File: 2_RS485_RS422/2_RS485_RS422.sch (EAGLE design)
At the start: 16 parts, among them IC1 74HCT02D, IC2 MAX485CSA, IC3 MAX485CSA, IC4 MAX489CSD, X1 AKL18X-10W, X8 ALLSERIALD

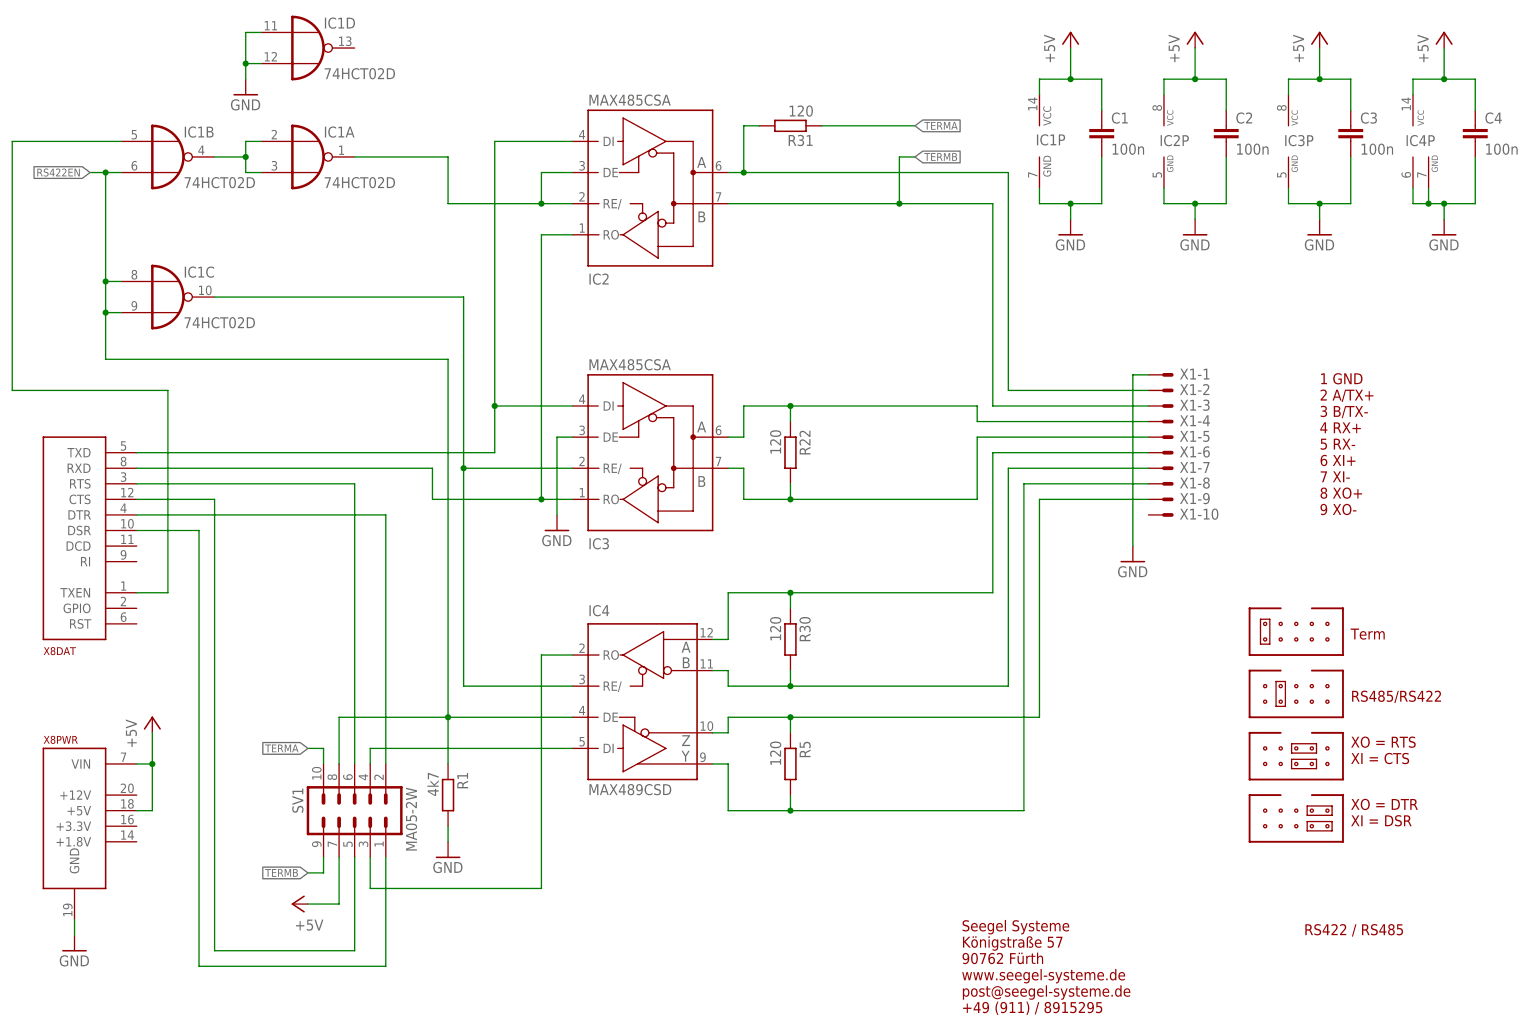
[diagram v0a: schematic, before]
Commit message: finish RS485 PCB
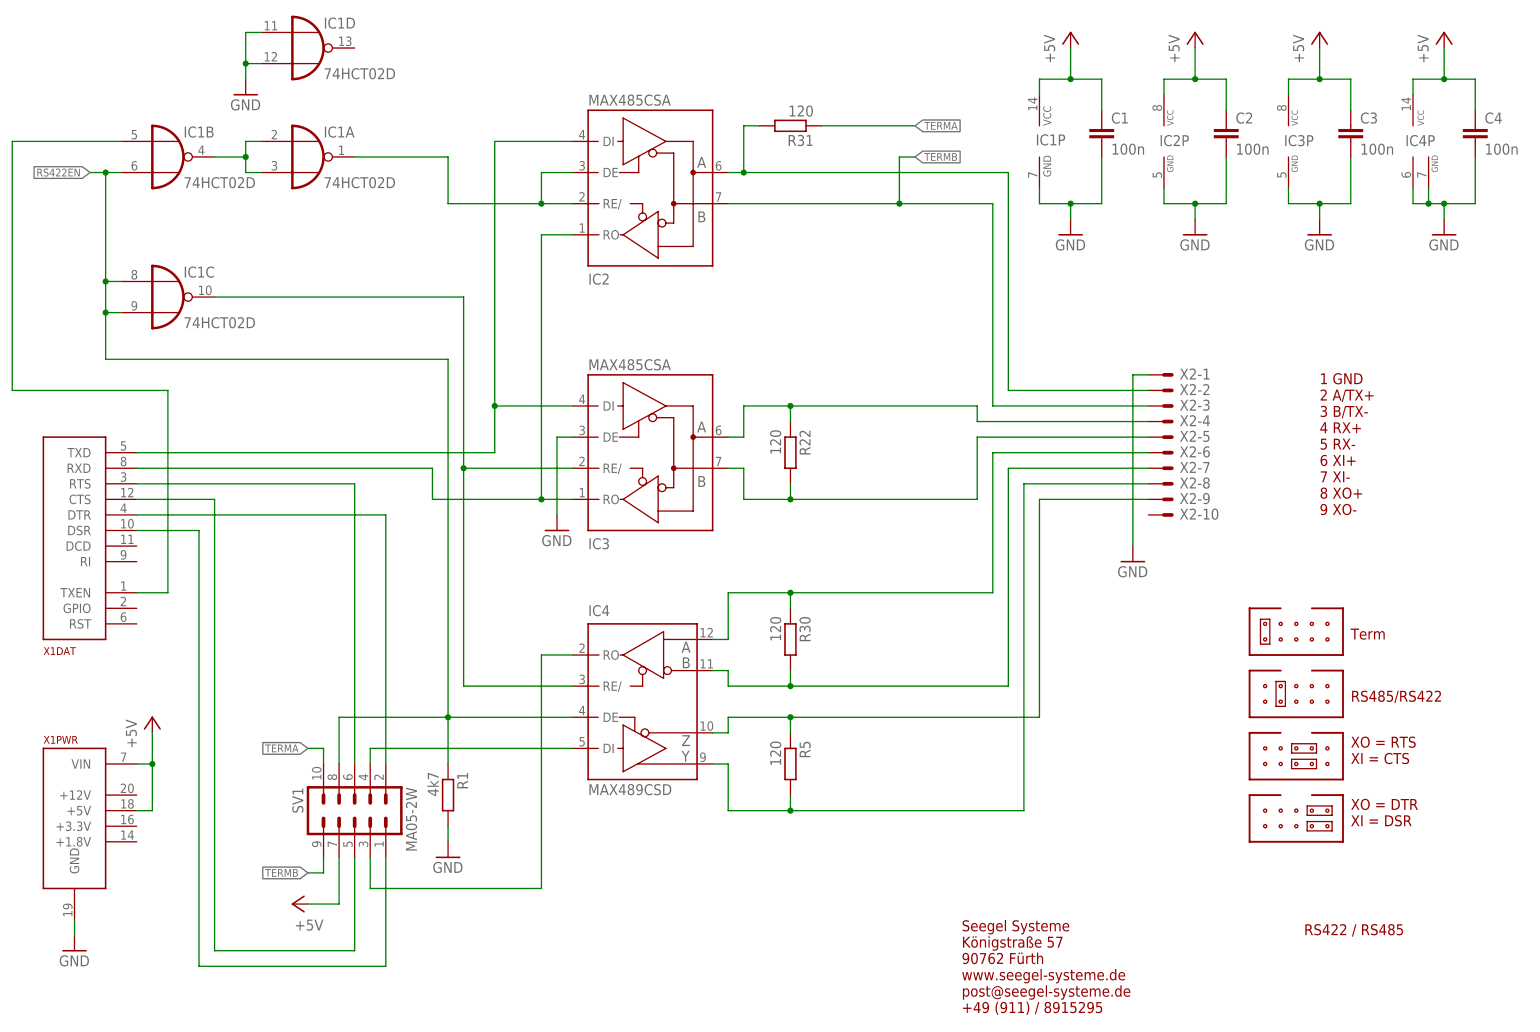
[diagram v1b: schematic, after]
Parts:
- removed X8: ALLSERIALD, AllSerial:ALLSERIALD
- added X2: AKL18X-10W, con-riacon_akl:AKL18X-10W
- X1: value AKL18X-10W -> ALLSERIALD; device con-riacon_akl:AKL18X-10W -> AllSerial:ALLSERIALD
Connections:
- net +5V: now also X1PWR.+5V, X1PWR.VIN; no longer X8PWR.+5V, X8PWR.VIN
- net GND: now also X1PWR.GND, X2-1.S; no longer X1-1.S, X8PWR.GND
- net N$1: now also X2-7.S; no longer X1-7.S
- net N$10: now also X2-8.S; no longer X1-8.S
- net N$2: now also X2-9.S; no longer X1-9.S
- net N$3: now also X2-2.S; no longer X1-2.S
- net N$37: now also X1DAT.TXEN; no longer X8DAT.TXEN
- net N$39: now also X2-6.S; no longer X1-6.S
- net N$40: now also X1DAT.CTS; no longer X8DAT.CTS
- net N$41: now also X2-5.S; no longer X1-5.S
- net N$43: now also X2-4.S; no longer X1-4.S
- net N$52: now also X1DAT.RXD; no longer X8DAT.RXD
- net N$53: now also X1DAT.TXD; no longer X8DAT.TXD
- net N$66: now also X1DAT.RTS; no longer X8DAT.RTS
- net N$67: now also X1DAT.DTR; no longer X8DAT.DTR
- net N$70: now also X1DAT.DSR; no longer X8DAT.DSR
- net TERMB: now also X2-3.S; no longer X1-3.S
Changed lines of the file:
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@@
 <?xml version="1.0" encoding="utf-8"?>
 <!DOCTYPE eagle SYSTEM "eagle.dtd">
-<eagle version="7.7.0">
+<eagle version="7.6.0">
 <drawing>
 <settings>
@@
 <part name="IC2" library="maxim" deviceset="MAX481CSA" device="" value="MAX485CSA"/>
 <part name="R22" library="rcl" deviceset="R-EU_" device="R0805" value="120"/>
-<part name="X1" library="con-riacon_akl" deviceset="AKL18X-10" device="W"/>
+<part name="X2" library="con-riacon_akl" deviceset="AKL18X-10" device="W"/>
 <part name="IC1" library="74xx-eu" deviceset="74*02" device="D" technology="HCT"/>
 <part name="R5" library="rcl" deviceset="R-EU_" device="R0805" value="120"/>
@@
 <part name="C3" library="rcl" deviceset="C-EU" device="C0805" value="100n"/>
 <part name="C4" library="rcl" deviceset="C-EU" device="C0805" value="100n"/>
-<part name="X8" library="AllSerial" deviceset="ALLSERIAL" device="D"/>
+<part name="X1" library="AllSerial" deviceset="ALLSERIAL" device="D"/>
 <part name="GND1" library="supply1" deviceset="GND" device=""/>
 <part name="GND2" library="supply1" deviceset="GND" device=""/>
@@
 <instance part="IC2" gate="G$1" x="111.76" y="142.24" rot="MR180"/>
 <instance part="R22" gate="G$1" x="134.62" y="99.06" rot="R270"/>
-<instance part="X1" gate="-1" x="195.58" y="111.76"/>
-<instance part="X1" gate="-2" x="195.58" y="109.22"/>
-<instance part="X1" gate="-3" x="195.58" y="106.68"/>
-<instance part="X1" gate="-4" x="195.58" y="104.14"/>
-<instance part="X1" gate="-5" x="195.58" y="101.6"/>
-<instance part="X1" gate="-6" x="195.58" y="99.06"/>
-<instance part="X1" gate="-7" x="195.58" y="96.52"/>
-<instance part="X1" gate="-8" x="195.58" y="93.98"/>
-<instance part="X1" gate="-9" x="195.58" y="91.44"/>
-<instance part="X1" gate="-10" x="195.58" y="88.9"/>
+<instance part="X2" gate="-1" x="195.58" y="111.76"/>
+<instance part="X2" gate="-2" x="195.58" y="109.22"/>
+<instance part="X2" gate="-3" x="195.58" y="106.68"/>
+<instance part="X2" gate="-4" x="195.58" y="104.14"/>
+<instance part="X2" gate="-5" x="195.58" y="101.6"/>
+<instance part="X2" gate="-6" x="195.58" y="99.06"/>
+<instance part="X2" gate="-7" x="195.58" y="96.52"/>
+<instance part="X2" gate="-8" x="195.58" y="93.98"/>
+<instance part="X2" gate="-9" x="195.58" y="91.44"/>
+<instance part="X2" gate="-10" x="195.58" y="88.9"/>
 <instance part="IC1" gate="B" x="33.02" y="147.32"/>
 <instance part="IC1" gate="A" x="55.88" y="147.32"/>
@@
 <instance part="C3" gate="G$1" x="226.06" y="152.4"/>
 <instance part="C4" gate="G$1" x="246.38" y="152.4"/>
-<instance part="X8" gate="DAT" x="17.78" y="83.82"/>
-<instance part="X8" gate="PWR" x="17.78" y="38.1"/>
+<instance part="X1" gate="DAT" x="17.78" y="83.82"/>
+<instance part="X1" gate="PWR" x="17.78" y="38.1"/>
 <instance part="IC1" gate="P" x="175.26" y="149.86"/>
 <instance part="GND1" gate="1" x="17.78" y="17.78"/>
@@
 <pinref part="R30" gate="G$1" pin="2"/>
 <wire x1="134.62" y1="63.5" x2="134.62" y2="60.96" width="0.1524" layer="91"/>
-<pinref part="X1" gate="-7" pin="S"/>
+<pinref part="X2" gate="-7" pin="S"/>
 <wire x1="193.04" y1="96.52" x2="170.18" y2="96.52" width="0.1524" layer="91"/>
 <wire x1="170.18" y1="96.52" x2="170.18" y2="60.96" width="0.1524" layer="91"/>
@@
 <wire x1="124.46" y1="55.88" x2="134.62" y2="55.88" width="0.1524" layer="91"/>
 <wire x1="134.62" y1="55.88" x2="134.62" y2="53.34" width="0.1524" layer="91"/>
-<pinref part="X1" gate="-9" pin="S"/>
+<pinref part="X2" gate="-9" pin="S"/>
 <wire x1="193.04" y1="91.44" x2="175.26" y2="91.44" width="0.1524" layer="91"/>
 <wire x1="175.26" y1="91.44" x2="175.26" y2="55.88" width="0.1524" layer="91"/>
@@
 <wire x1="124.46" y1="40.64" x2="134.62" y2="40.64" width="0.1524" layer="91"/>
 <wire x1="134.62" y1="40.64" x2="134.62" y2="43.18" width="0.1524" layer="91"/>
-<pinref part="X1" gate="-8" pin="S"/>
+<pinref part="X2" gate="-8" pin="S"/>
 <wire x1="193.04" y1="93.98" x2="172.72" y2="93.98" width="0.1524" layer="91"/>
 <wire x1="172.72" y1="93.98" x2="172.72" y2="40.64" width="0.1524" layer="91"/>
@@
 <wire x1="124.46" y1="76.2" x2="134.62" y2="76.2" width="0.1524" layer="91"/>
 <wire x1="134.62" y1="76.2" x2="134.62" y2="73.66" width="0.1524" layer="91"/>
-<pinref part="X1" gate="-6" pin="S"/>
+<pinref part="X2" gate="-6" pin="S"/>
 <wire x1="193.04" y1="99.06" x2="167.64" y2="99.06" width="0.1524" layer="91"/>
 <wire x1="167.64" y1="99.06" x2="167.64" y2="76.2" width="0.1524" layer="91"/>
@@
 <wire x1="165.1" y1="101.6" x2="193.04" y2="101.6" width="0.1524" layer="91"/>
 <junction x="134.62" y="91.44"/>
-<pinref part="X1" gate="-5" pin="S"/>
+<pinref part="X2" gate="-5" pin="S"/>
 </segment>
 </net>
@@
 <wire x1="165.1" y1="106.68" x2="165.1" y2="104.14" width="0.1524" layer="91"/>
 <junction x="134.62" y="106.68"/>
-<pinref part="X1" gate="-4" pin="S"/>
+<pinref part="X2" gate="-4" pin="S"/>
 <wire x1="165.1" y1="104.14" x2="193.04" y2="104.14" width="0.1524" layer="91"/>
 </segment>
@@
 <wire x1="93.98" y1="91.44" x2="76.2" y2="91.44" width="0.1524" layer="91"/>
 <wire x1="76.2" y1="91.44" x2="76.2" y2="96.52" width="0.1524" layer="91"/>
-<pinref part="X8" gate="DAT" pin="RXD"/>
+<pinref part="X1" gate="DAT" pin="RXD"/>
 <wire x1="27.94" y1="96.52" x2="76.2" y2="96.52" width="0.1524" layer="91"/>
 </segment>
@@
 <wire x1="86.36" y1="106.68" x2="99.06" y2="106.68" width="0.1524" layer="91"/>
 <junction x="86.36" y="106.68"/>
-<pinref part="X8" gate="DAT" pin="TXD"/>
+<pinref part="X1" gate="DAT" pin="TXD"/>
 <wire x1="27.94" y1="99.06" x2="86.36" y2="99.06" width="0.1524" layer="91"/>
 <wire x1="86.36" y1="99.06" x2="86.36" y2="106.68" width="0.1524" layer="91"/>
@@
 <pinref part="SV1" gate="G$1" pin="6"/>
 <wire x1="63.5" y1="93.98" x2="63.5" y2="48.26" width="0.1524" layer="91"/>
-<pinref part="X8" gate="DAT" pin="RTS"/>
+<pinref part="X1" gate="DAT" pin="RTS"/>
 <wire x1="27.94" y1="93.98" x2="63.5" y2="93.98" width="0.1524" layer="91"/>
 </segment>
@@
 <wire x1="63.5" y1="17.78" x2="40.64" y2="17.78" width="0.1524" layer="91"/>
 <wire x1="40.64" y1="17.78" x2="40.64" y2="91.44" width="0.1524" layer="91"/>
-<pinref part="X8" gate="DAT" pin="CTS"/>
+<pinref part="X1" gate="DAT" pin="CTS"/>
 <wire x1="40.64" y1="91.44" x2="27.94" y2="91.44" width="0.1524" layer="91"/>
 </segment>
@@
 <wire x1="7.62" y1="109.22" x2="33.02" y2="109.22" width="0.1524" layer="91"/>
 <wire x1="33.02" y1="109.22" x2="33.02" y2="76.2" width="0.1524" layer="91"/>
-<pinref part="X8" gate="DAT" pin="TXEN"/>
+<pinref part="X1" gate="DAT" pin="TXEN"/>
 <wire x1="33.02" y1="76.2" x2="27.94" y2="76.2" width="0.1524" layer="91"/>
 </segment>
@@
 <wire x1="68.58" y1="15.24" x2="38.1" y2="15.24" width="0.1524" layer="91"/>
 <wire x1="38.1" y1="15.24" x2="38.1" y2="86.36" width="0.1524" layer="91"/>
-<pinref part="X8" gate="DAT" pin="DSR"/>
+<pinref part="X1" gate="DAT" pin="DSR"/>
 <wire x1="38.1" y1="86.36" x2="27.94" y2="86.36" width="0.1524" layer="91"/>
 </segment>
@@
 <net name="N$67" class="0">
 <segment>
-<pinref part="X8" gate="DAT" pin="DTR"/>
+<pinref part="X1" gate="DAT" pin="DTR"/>
 <pinref part="SV1" gate="G$1" pin="2"/>
 <wire x1="27.94" y1="88.9" x2="68.58" y2="88.9" width="0.1524" layer="91"/>
@@
 <net name="GND" class="0">
 <segment>
-<pinref part="X8" gate="PWR" pin="GND"/>
+<pinref part="X1" gate="PWR" pin="GND"/>
 <wire x1="17.78" y1="20.32" x2="17.78" y2="22.86" width="0.1524" layer="91"/>
 <pinref part="GND1" gate="1" pin="GND"/>
@@
 </segment>
 <segment>
-<pinref part="X1" gate="-1" pin="S"/>
+<pinref part="X2" gate="-1" pin="S"/>
 <pinref part="GND8" gate="1" pin="GND"/>
 <wire x1="193.04" y1="111.76" x2="190.5" y2="111.76" width="0.1524" layer="91"/>
@@
 <net name="+5V" class="0">
 <segment>
-<pinref part="X8" gate="PWR" pin="+5V"/>
+<pinref part="X1" gate="PWR" pin="+5V"/>
 <wire x1="27.94" y1="40.64" x2="30.48" y2="40.64" width="0.1524" layer="91"/>
 <wire x1="30.48" y1="40.64" x2="30.48" y2="48.26" width="0.1524" layer="91"/>
-<pinref part="X8" gate="PWR" pin="VIN"/>
+<pinref part="X1" gate="PWR" pin="VIN"/>
 <wire x1="30.48" y1="48.26" x2="30.48" y2="53.34" width="0.1524" layer="91"/>
 <wire x1="27.94" y1="48.26" x2="30.48" y2="48.26" width="0.1524" layer="91"/>
@@
 <wire x1="127" y1="144.78" x2="170.18" y2="144.78" width="0.1524" layer="91"/>
 <wire x1="170.18" y1="144.78" x2="170.18" y2="109.22" width="0.1524" layer="91"/>
-<pinref part="X1" gate="-2" pin="S"/>
+<pinref part="X2" gate="-2" pin="S"/>
 <wire x1="170.18" y1="109.22" x2="193.04" y2="109.22" width="0.1524" layer="91"/>
 <pinref part="R31" gate="G$1" pin="2"/>
@@
 <wire x1="152.4" y1="139.7" x2="167.64" y2="139.7" width="0.1524" layer="91"/>
 <wire x1="167.64" y1="139.7" x2="167.64" y2="106.68" width="0.1524" layer="91"/>
-<pinref part="X1" gate="-3" pin="S"/>
+<pinref part="X2" gate="-3" pin="S"/>
 <wire x1="167.64" y1="106.68" x2="193.04" y2="106.68" width="0.1524" layer="91"/>
 <wire x1="152.4" y1="139.7" x2="152.4" y2="147.32" width="0.1524" layer="91"/>

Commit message: change to libv2
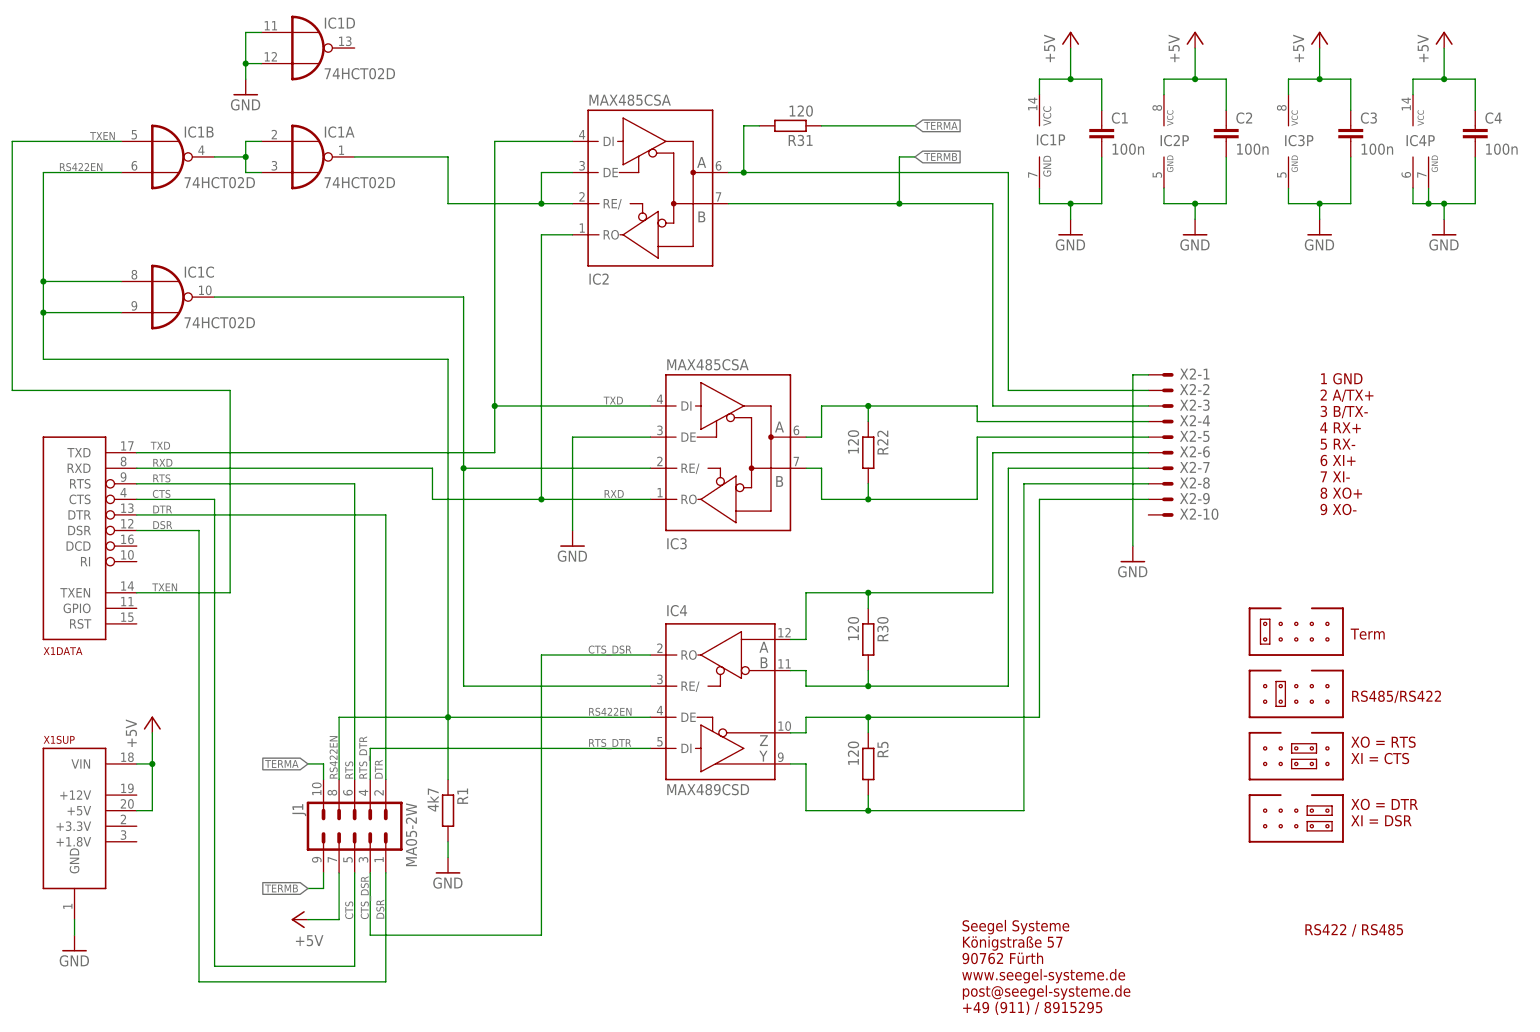
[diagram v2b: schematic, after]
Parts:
- removed SV1: MA05-2W, con-lstb:MA05-2W
- added J1: MA05-2W, con-lstb:MA05-2W
- X1: value ALLSERIALD -> ALLSERIALSLAVE; device AllSerial:ALLSERIALD -> AllSerialv2:ALLSERIALSLAVE
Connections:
- removed net N$37: IC1B.I0, X1DAT.TXEN
- removed net N$40: SV1.5, X1DAT.CTS
- removed net N$52: IC2G$1.RO, IC3G$1.RO, X1DAT.RXD
- removed net N$53: IC2G$1.DI, IC3G$1.DI, X1DAT.TXD
- removed net N$66: SV1.6, X1DAT.RTS
- removed net N$67: SV1.2, X1DAT.DTR
- removed net N$68: IC4G$1.DI, SV1.4
- removed net N$69: IC4G$1.RO, SV1.3
- removed net N$70: SV1.1, X1DAT.DSR
- new net CTS: J1.5, X1DATA.CTS
- new net CTS_DSR: IC4G$1.RO, J1.3
- new net DSR: J1.1, X1DATA.DSR
- new net DTR: J1.2, X1DATA.DTR
- new net RTS: J1.6, X1DATA.RTS
- new net RTS_DTR: IC4G$1.DI, J1.4
- new net RXD: IC2G$1.RO, IC3G$1.RO, X1DATA.RXD
- new net TXD: IC2G$1.DI, IC3G$1.DI, X1DATA.TXD
- new net TXEN: IC1B.I0, X1DATA.TXEN
- net +5V: now also J1.7, X1SUP.+5V, X1SUP.VIN; no longer SV1.7, X1PWR.+5V, X1PWR.VIN
- net GND: now also X1SUP.GND; no longer X1PWR.GND
- net RS422EN: now also J1.8; no longer SV1.8
- net TERMA: now also J1.10; no longer SV1.10
- net TERMB: now also J1.9; no longer SV1.9
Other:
- moved on the sheet: IC3, IC4, R1, R22, R30, R5
